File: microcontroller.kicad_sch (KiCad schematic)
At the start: 58 parts, among them J6 Conn_01x03_Pin, J7 Conn_01x05_Pin, SW1 SW_SPST, SW2 SW_SPST, U3 W25Q16JVSS, U4 W25Q16JVSS, U6 RP2040, Y1 12MHz/10pF, Y2 12MHz/10pF

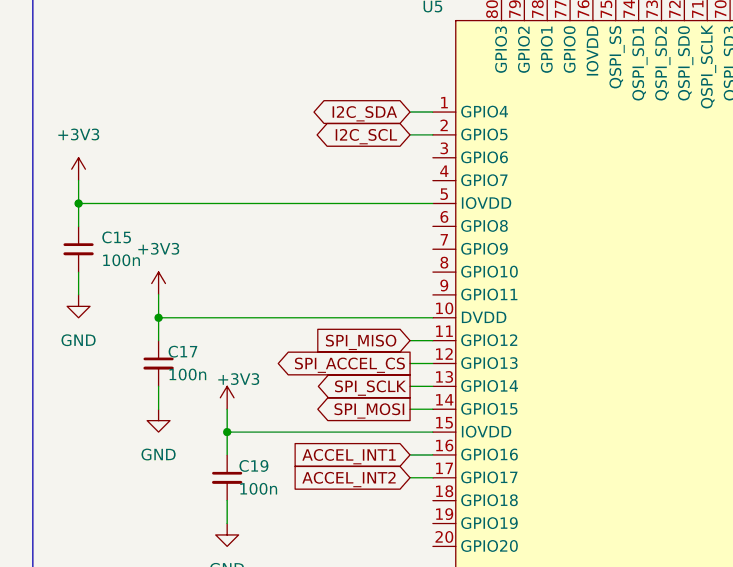
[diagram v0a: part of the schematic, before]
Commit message: feat: adds footprints and new light sensor
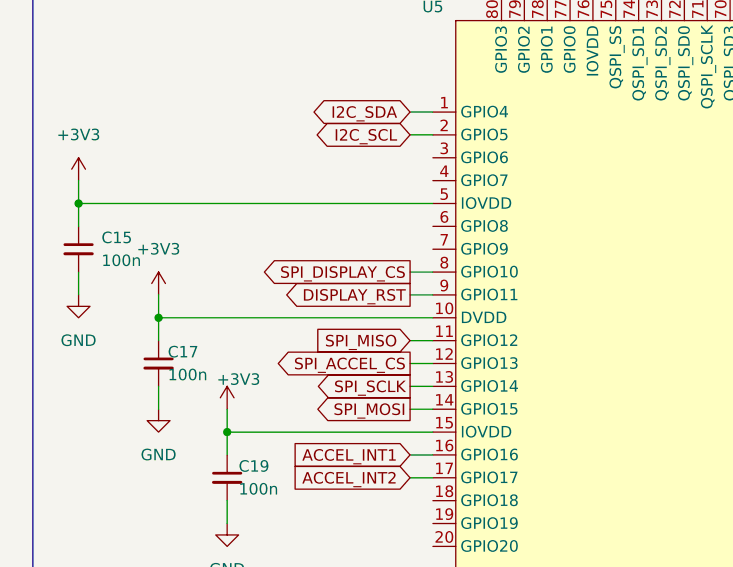
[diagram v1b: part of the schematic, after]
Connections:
- net SPI_DISPLAY_CS: now reaches U5.8 (GPIO10)
- net DISPLAY_RST: now reaches U5.9 (GPIO11)
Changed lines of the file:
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@@
 	(wire
 		(pts
+			(xy 57.15 104.14) (xy 59.69 104.14)
+		)
+		(stroke
+			(width 0)
+			(type default)
+		)
+	)
+	(wire
+		(pts
 			(xy 241.3 55.88) (xy 243.84 55.88)
 		)
@@
 	(wire
 		(pts
+			(xy 57.15 106.68) (xy 59.69 106.68)
+		)
+		(stroke
+			(width 0)
+			(type default)
+		)
+	)
+	(wire
+		(pts
 			(xy 363.22 147.32) (xy 384.81 147.32)
 		)
@@
 				(hide yes)
 			)
+		)
+	)
+	(global_label "DISPLAY_RST"
+		(shape output)
+		(at 57.15 106.68 180)
+		(fields_autoplaced yes)
+		(effects
+			(font
+				(size 1.27 1.27)
+			)
+			(justify right)
+		)
+		(property "Intersheetrefs" "${INTERSHEET_REFS}"
+			(at 42.1905 106.68 0)
+			(effects
+				(font
+					(size 1.27 1.27)
+				)
+				(justify right)
+				(hide yes)
+			)
+		)
+	)
+	(global_label "SPI_DISPLAY_CS"
+		(shape output)
+		(at 57.15 104.14 180)
+		(fields_autoplaced yes)
+		(effects
+			(font
+				(size 1.27 1.27)
+			)
+			(justify right)
+		)
+		(property "Intersheetrefs" "${INTERSHEET_REFS}"
+			(at 39.1062 104.14 0)
+			(effects
+				(font
+					(size 1.27 1.27)
+				)
+				(justify right)
+				(hide yes)
+			)

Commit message: feat: connects all global labels
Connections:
- net LDR_ADC: now also U5.53 (GPIO42_ADC2); no longer U5.57 (GPIO46_ADC6)
- net POTENTIOMETER1_ADC: now also U5.49 (GPIO40_ADC0); no longer U5.55 (GPIO44_ADC4)
- net POTENTIOMETER2_ADC: now also U5.52 (GPIO41_ADC1); no longer U5.53 (GPIO42_ADC2)
- net RP2350_RX/BT_TX: now also U5.21 (GPIO21)
- net RP2350_TX/BT_RX: now also U5.20 (GPIO20)
- net BUTTON1_GPIO: now reaches U5.22 (GPIO22)
- net BUTTON2_GPIO: now reaches U5.23 (GPIO23)
- net BUTTON3_GPIO: now reaches U5.25 (GPIO24)
- net BUTTON4_GPIO: now reaches U5.26 (GPIO25)
- net ~{IR_EMITTER_GPIO}: now reaches U5.38 (GPIO30)
- net MOSFET_GPIO: now reaches U5.39 (GPIO31)
- net BUZZER_GPIO: now reaches U5.40 (GPIO32)
- net IR_REC_GPIO: now reaches U5.42 (GPIO33)
- net MICROPHONE_ADC: now reaches U5.54 (GPIO43_ADC3)
- net DISPLAY_EN: now reaches U5.7 (GPIO9)
- net ~{LED_BLUE_GPIO}: now reaches U5.77 (GPIO0)
- net ~{LED_GREEN_GPIO}: now reaches U5.78 (GPIO1)
- net ~{LED_YELLOW_GPIO}: now reaches U5.79 (GPIO2)
- net ~{LED_RED_GPIO}: now reaches U5.80 (GPIO3)
- net SPI_ACCEL_CS renamed ~{SPI_ACCEL_CS}
- net SPI_DISPLAY_CS renamed ~{SPI_DISPLAY_CS}
- no-connect marks 0 -> 26
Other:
- note added: "Communication Headers"
- note added: "External GPIOs"
- note removed: "External Headers"
- moved on the sheet: C32, C33, C8

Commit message: chore: makes changes for DRC check compliance
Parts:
- L1: footprint (none) -> Inductor_SMD:L_0805_2012Metric_Pad1.05x1.20mm_HandSolder
- R17: renamed from R12; MPN (none) -> RC0402JR-0727RL
- R18: renamed from R13; MPN (none) -> RC0402JR-0727RL
- R20: renamed from R14; MPN (none) -> RC0402JR-0727RL
- R21: renamed from R15; MPN (none) -> RC0402JR-0727RL
- renumbered C21 to C10, C22 to C11, C23 to C12, C24 to C13, C25 to C14, C26 to C15, C27 to C16, C28 to C17, C29 to C18, C30 to C19, C31 to C20, C39 to C21, C12 to C22, C13 to C23, C14 to C24, C40 to C25, C15 to C26, C16 to C27, C17 to C28, C37 to C29, C18 to C30, C38 to C31, C19 to C32, C20 to C33, C32 to C35, C33 to C36, C35 to C37, C36 to C38, C10 to C39, C11 to C40, C8 to C6, C9 to C7, C53 to C8, C54 to C9, D10 to D8, J6 to J4, J7 to J5, R17 to R16, R9 to R19, R18 to R22, R16 to R23, R30 to R24, R10 to R25, R11 to R26, SW1 to SW2, SW2 to SW3, U6 to U3, U5 to U4, U3 to U5, U4 to U6, Y2 to Y1, Y1 to Y2

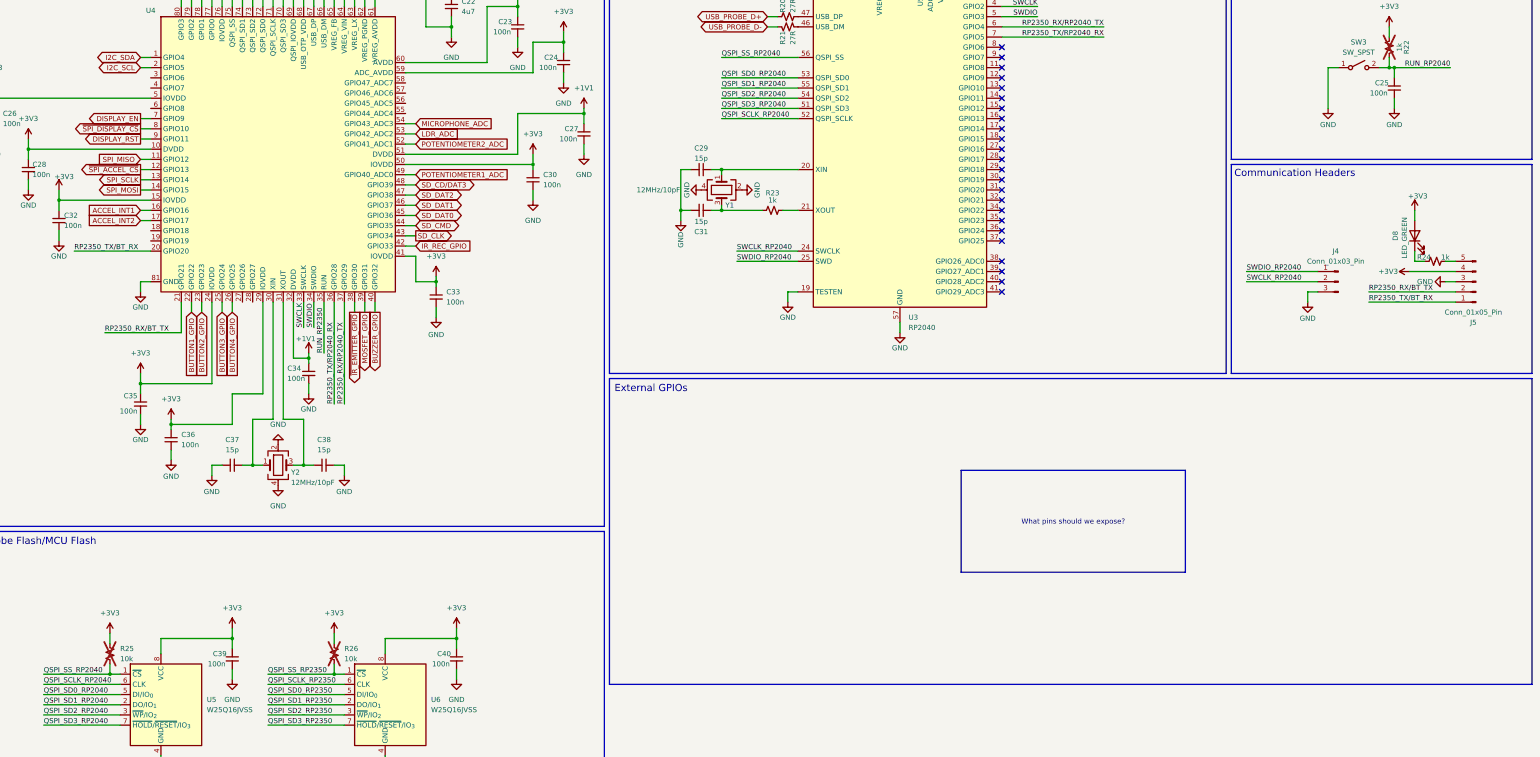
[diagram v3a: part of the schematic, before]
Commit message: feat: adds testpoints
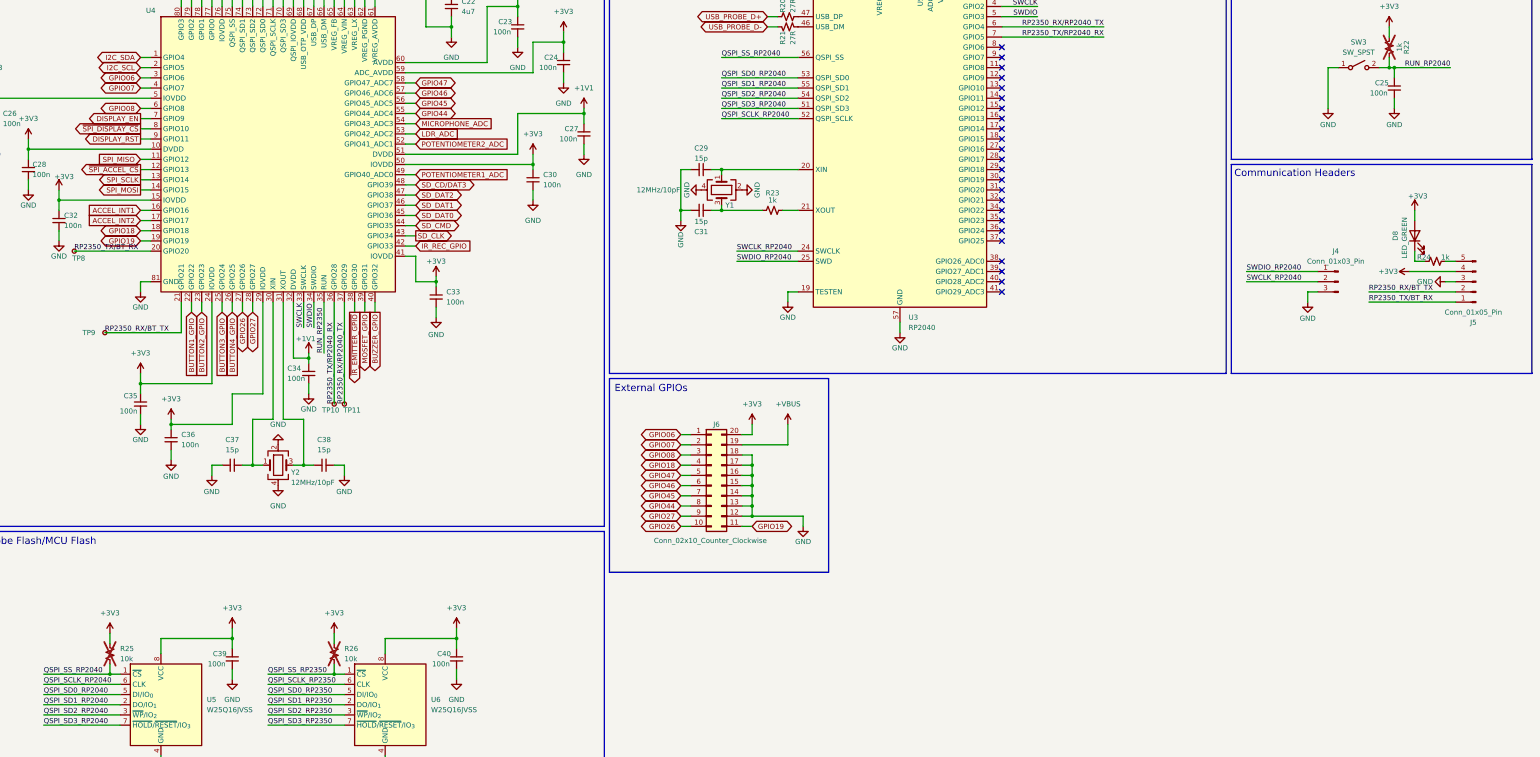
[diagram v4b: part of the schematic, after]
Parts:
- added J6: Conn_02x10_Counter_Clockwise, Connector_PinSocket_2.54mm:PinSocket_2x10_P2.54mm_Vertical, symbol Connector_Generic:Conn_02x10_Counter_Clockwise
- added TP10, TP11, TP8, TP9: TestPoint_Small, TestPoint:TestPoint_Pad_D1.0mm, symbol Connector:TestPoint_Small
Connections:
- net +3V3: now also J6.20 (Pin_20)
- net GND: now also J6.12 (Pin_12), J6.13 (Pin_13), J6.14 (Pin_14), J6.15 (Pin_15), J6.16 (Pin_16), J6.17 (Pin_17), J6.18 (Pin_18)
- net RP2350_RX/BT_TX: now also TP9.1
- net RP2350_RX/RP2040_TX: now also TP11.1
- net RP2350_TX/BT_RX: now also TP8.1
- net RP2350_TX/RP2040_RX: now also TP10.1
- net GPIO18: now reaches U4.18 (GPIO18)
- net GPIO18: now also J6.4 (Pin_4)
- net GPIO19: now reaches U4.19 (GPIO19)
- net GPIO19: now also J6.11 (Pin_11)
- net GPIO26: now reaches U4.27 (GPIO26)
- net GPIO26: now also J6.10 (Pin_10)
- net GPIO27: now reaches U4.28 (GPIO27)
- net GPIO27: now also J6.9 (Pin_9)
- net GPIO06: now reaches U4.3 (GPIO6)
- net GPIO06: now also J6.1 (Pin_1)
- net GPIO07: now reaches U4.4 (GPIO7)
- net GPIO07: now also J6.2 (Pin_2)
- net GPIO44: now reaches U4.55 (GPIO44_ADC4)
- net GPIO44: now also J6.8 (Pin_8)
- net GPIO45: now reaches U4.56 (GPIO45_ADC5)
- net GPIO45: now also J6.7 (Pin_7)
- net GPIO46: now reaches U4.57 (GPIO46_ADC6)
- net GPIO46: now also J6.6 (Pin_6)
- net GPIO47: now reaches U4.58 (GPIO47_ADC7)
- net GPIO47: now also J6.5 (Pin_5)
- net GPIO08: now reaches U4.6 (GPIO8)
- net GPIO08: now also J6.3 (Pin_3)
- new net +VBUS: J6.19 (Pin_19)

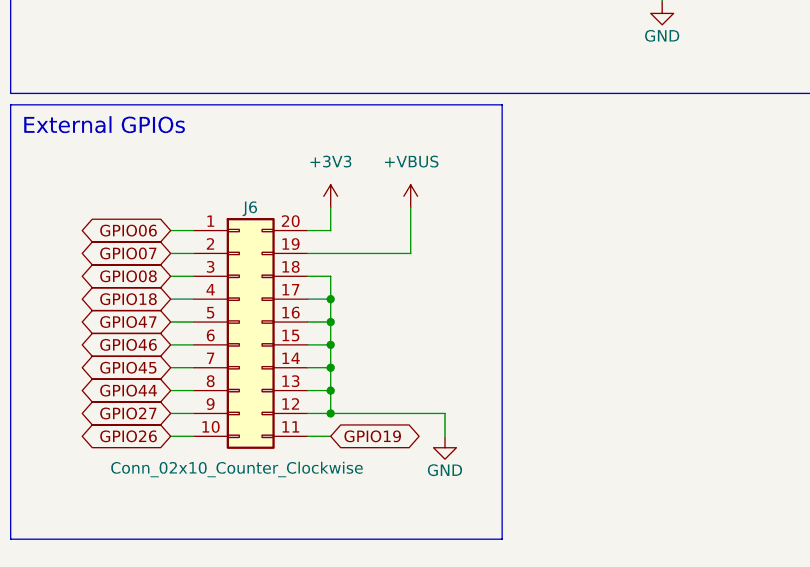
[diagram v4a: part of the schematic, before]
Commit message: wip: moves components around on PCB
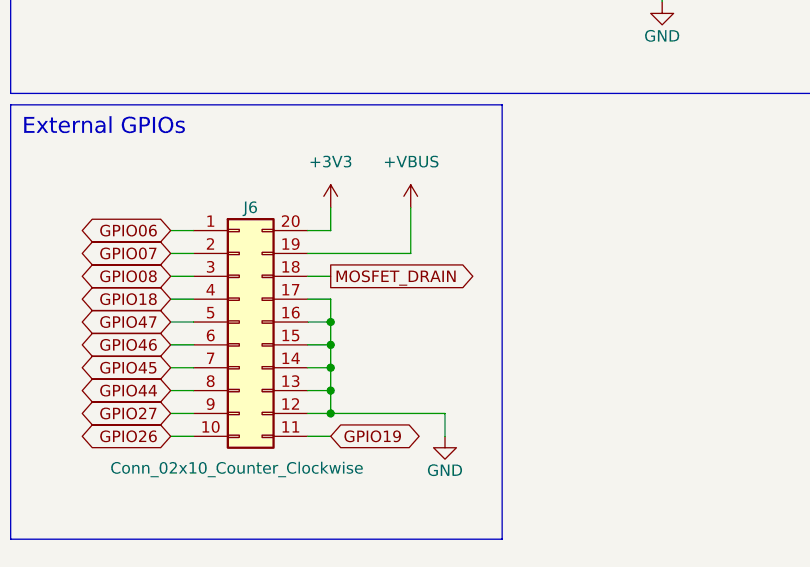
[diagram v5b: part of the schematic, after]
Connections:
- net GND: no longer J6.18 (Pin_18)
- new net MOSFET_DRAIN: J6.18 (Pin_18)
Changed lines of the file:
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@@
 	)
 	(junction
-		(at 209.55 187.96)
-		(diameter 0)
-		(color 0 0 0 0)
-	)
-	(junction
 		(at 369.57 88.9)
 		(diameter 0)
@@
 	(wire
 		(pts
-			(xy 209.55 185.42) (xy 209.55 187.96)
-		)
-		(stroke
-			(width 0)
-			(type default)
-		)
-	)
-	(wire
-		(pts
 			(xy 271.78 78.74) (xy 297.18 78.74)
 		)
@@
 	(wire
 		(pts
-			(xy 207.01 185.42) (xy 209.55 185.42)
-		)
-		(stroke
-			(width 0)
-			(type default)
-		)
-	)
-	(wire
-		(pts
 			(xy 36.83 129.54) (xy 36.83 132.08)
 		)
@@
 	(wire
 		(pts
+			(xy 209.55 185.42) (xy 207.01 185.42)
+		)
+		(stroke
+			(width 0)
+			(type default)
+		)
+	)
+	(wire
+		(pts
 			(xy 205.74 137.16) (xy 220.98 137.16)
 		)
@@
 			(effects
 				(font
+					(size 1.27 1.27)
+				)
+				(justify left)
+				(hide yes)
+			)
+		)
+	)
+	(global_label "MOSFET_DRAIN"
+		(shape output)
+		(at 209.55 185.42 0)
+		(fields_autoplaced yes)
+		(effects
+			(font
+				(size 1.27 1.27)
+			)
+			(justify left)
+		)
+		(property "Intersheetrefs" "${INTERSHEET_REFS}"
+			(at 226.2633 185.42 0)
+			(effects
+				(font

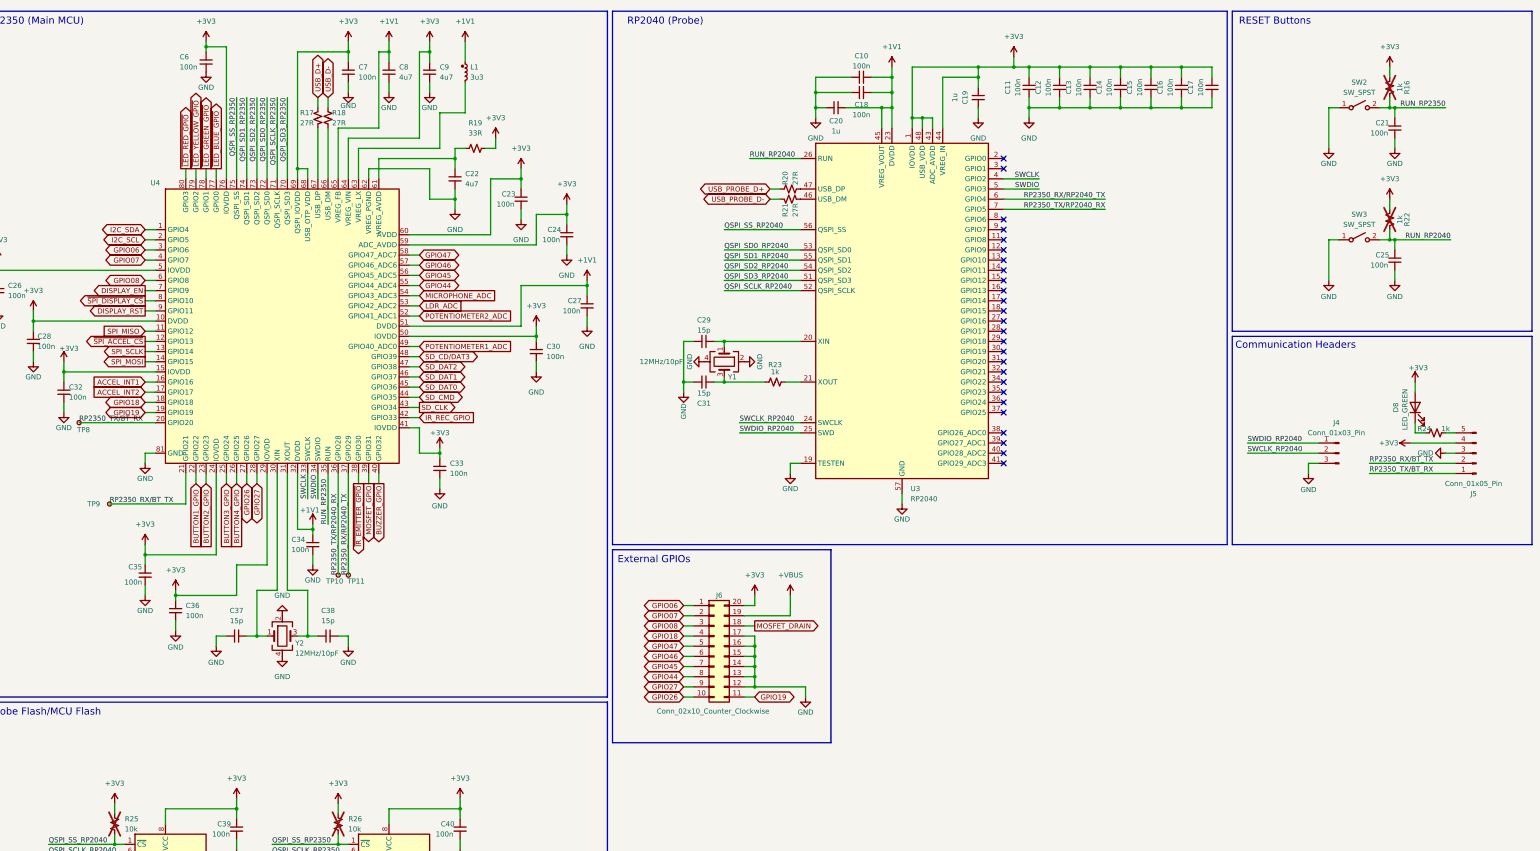
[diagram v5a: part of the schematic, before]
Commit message: feat:  adds requested components
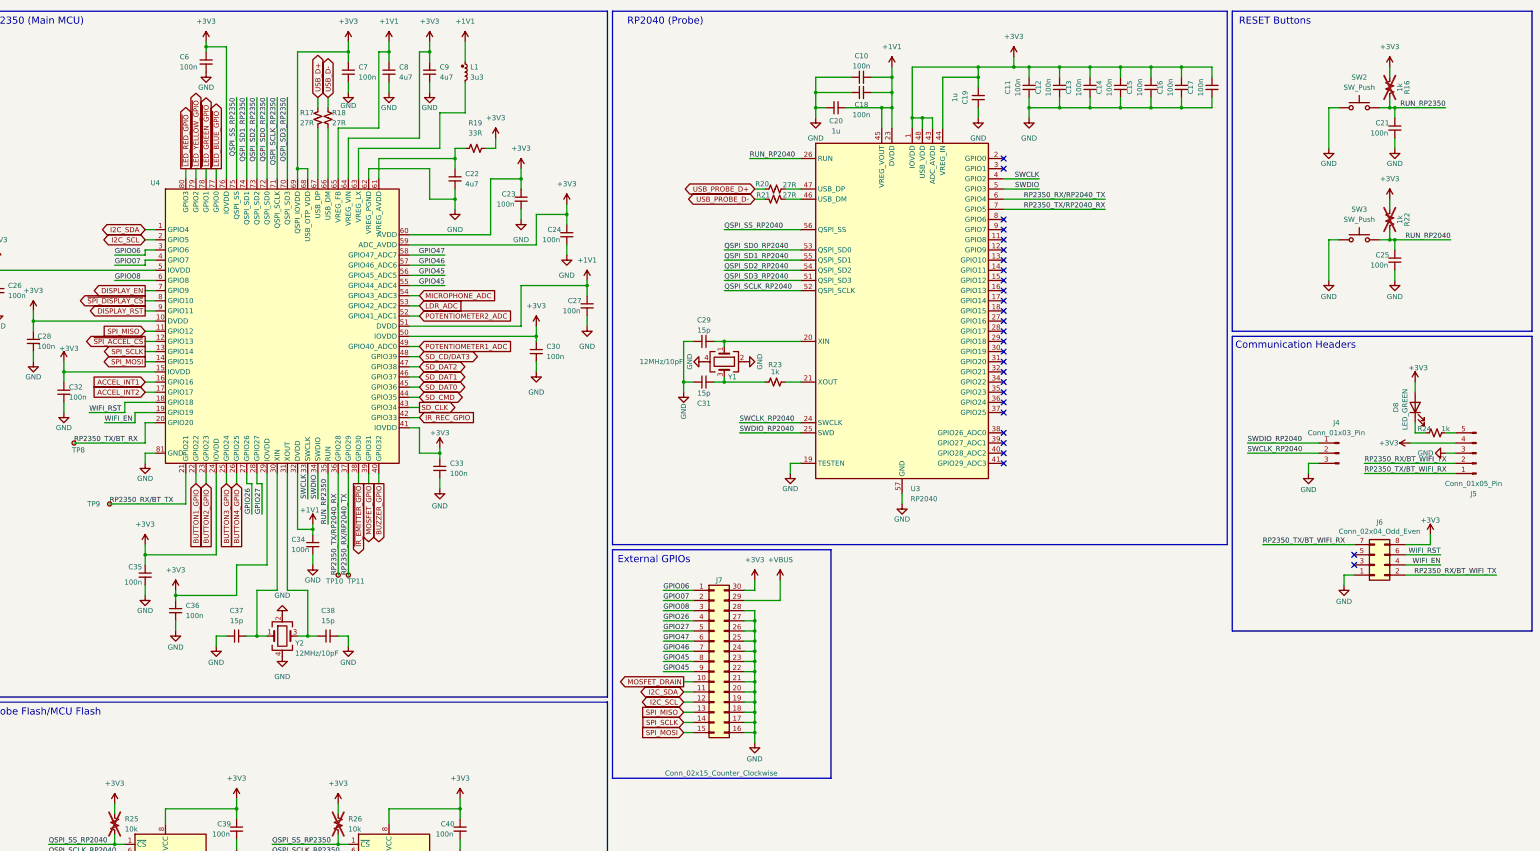
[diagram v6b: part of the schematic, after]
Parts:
- removed J6: Conn_02x10_Counter_Clockwise, Connector_PinSocket_2.54mm:PinSocket_2x10_P2.54mm_Vertical, symbol Connector_Generic:Conn_02x10_Counter_Clockwise
- removed SW2, SW3: SW_SPST, microcontroller:SMD Button, symbol Switch:SW_SPST
- added J6: Conn_02x04_Odd_Even, Connector_PinSocket_2.54mm:PinSocket_2x04_P2.54mm_Vertical, symbol Connector_Generic:Conn_02x04_Odd_Even
- added J7: Conn_02x15_Counter_Clockwise, Connector_PinHeader_2.54mm:PinHeader_2x15_P2.54mm_Vertical, symbol Connector_Generic:Conn_02x15_Counter_Clockwise
- added SW2, SW3: SW_Push, Button_Switch_THT:SW_PUSH_6mm_H4.3mm, symbol Switch:SW_Push
- J4: footprint Connector:FanPinHeader_1x03_P2.54mm_Vertical -> Connector_PinHeader_2.54mm:PinHeader_1x03_P2.54mm_Vertical
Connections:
- net GPIO44 is gone; now on net GPIO45: U4.55 (GPIO44_ADC4)
- net +3V3: now also J6.8 (Pin_8), J7.30 (Pin_30)
- net +VBUS: now also J7.29 (Pin_29)
- net GND: now also J6.1 (Pin_1), J7.16 (Pin_16), J7.17 (Pin_17), J7.18 (Pin_18), J7.19 (Pin_19), J7.20 (Pin_20), J7.21 (Pin_21), J7.22 (Pin_22), J7.23 (Pin_23), J7.24 (Pin_24), J7.25 (Pin_25), J7.26 (Pin_26), J7.27 (Pin_27), J7.28 (Pin_28), SW2.1, SW3.1
- net GPIO06: now also J7.1 (Pin_1)
- net GPIO07: now also J7.2 (Pin_2)
- net GPIO08: now also J7.3 (Pin_3)
- net GPIO26: now also J7.4 (Pin_4)
- net GPIO27: now also J7.5 (Pin_5)
- net GPIO45: now also J7.8 (Pin_8), J7.9 (Pin_9)
- net GPIO46: now also J7.7 (Pin_7)
- net GPIO47: now also J7.6 (Pin_6)
- net I2C_SCL: now also J7.12 (Pin_12)
- net I2C_SDA: now also J7.11 (Pin_11)
- net MOSFET_DRAIN: now also J7.10 (Pin_10)
- net RP2350_RX/BT_TX: no longer J5.2 (Pin_2)
- net RP2350_TX/BT_RX: no longer J5.1 (Pin_1)
- net RUN_RP2040: now also SW3.2
- net RUN_RP2350: now also SW2.2
- net SPI_MISO: now also J7.13 (Pin_13)
- net SPI_MOSI: now also J7.15 (Pin_15)
- net SPI_SCLK: now also J7.14 (Pin_14)
- net GPIO18 renamed WIFI_RST
- net WIFI_RST: now also J6.6 (Pin_6)
- net GPIO19 renamed WIFI_EN
- net WIFI_EN: now also J6.4 (Pin_4)
- new net RP2350_RX/BT_WIFI_TX: J5.2 (Pin_2), J6.2 (Pin_2)
- new net RP2350_TX/BT_WIFI_RX: J5.1 (Pin_1), J6.7 (Pin_7)
- no-connect marks 26 -> 28
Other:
- moved on the sheet: R20, R21, TP8
